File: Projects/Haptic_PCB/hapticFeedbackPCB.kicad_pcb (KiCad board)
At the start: 2 copper layers, 70.5 x 55 mm, 18 parts, among them J1 430450212, J2 430450212, M1 Motor_DC, M2 Motor_DC, M3 Motor_DC, Q1 NPN, Q2 NPN, Q3 NPN

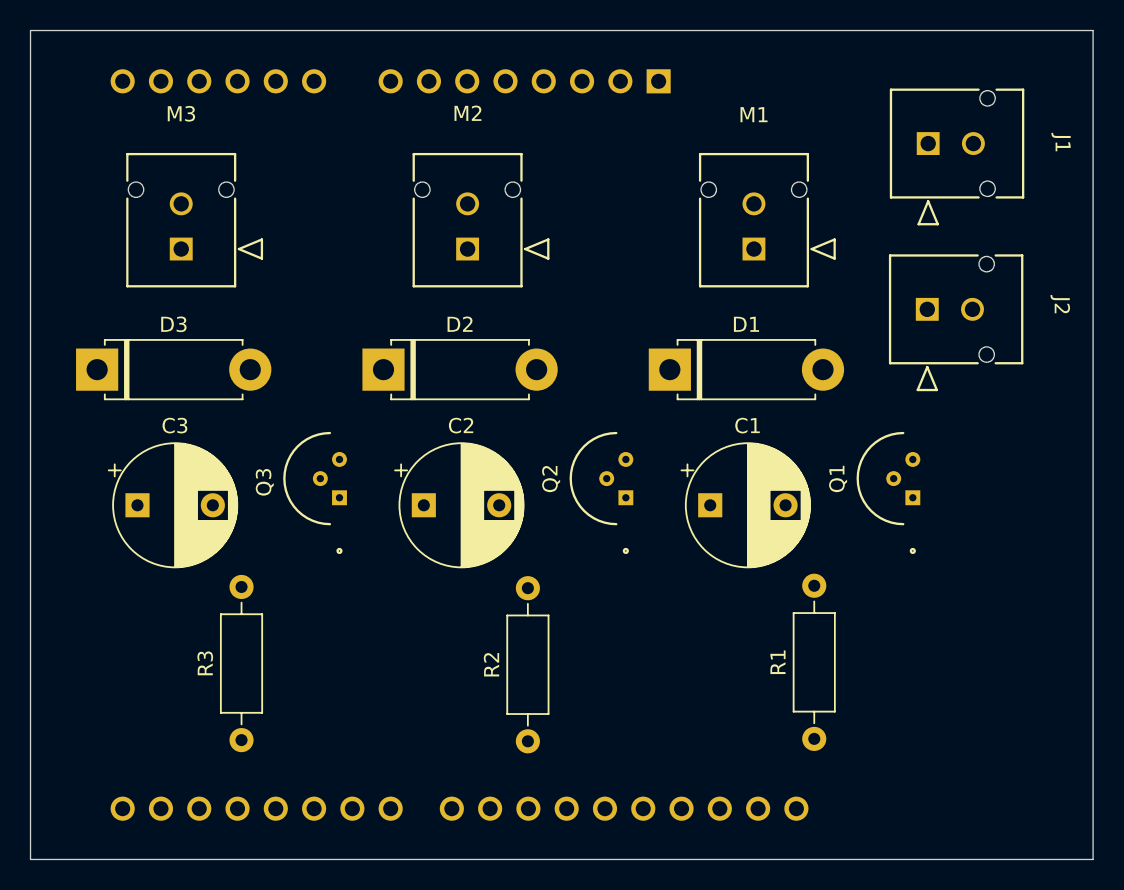
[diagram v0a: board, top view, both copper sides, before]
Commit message: Added PCB traces.
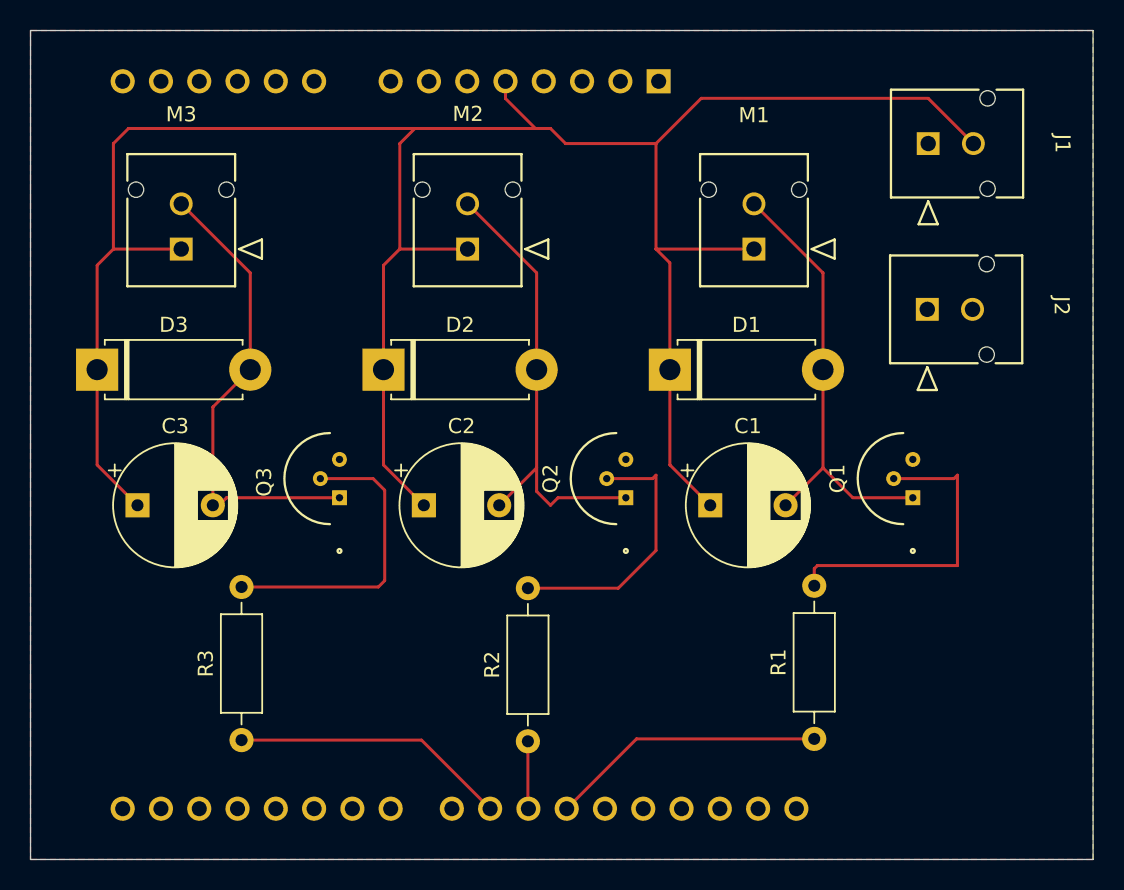
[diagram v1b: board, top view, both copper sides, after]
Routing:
- net +5V: track 0.00 -> 157.8 mm
- net Net-(D3-A): track 0.00 -> 31.5 mm
- net Net-(D2-A): track 0.00 -> 31.0 mm
- net Net-(D1-A): track 0.00 -> 30.2 mm
- net Net-(Q1-B): track 0.00 -> 21.0 mm
- net Net-(Q3-B): track 0.00 -> 20.3 mm
- net Net-(A1-D9): track 0.00 -> 18.4 mm
- net Net-(A1-D11): track 0.00 -> 18.3 mm
- net Net-(Q2-B): track 0.00 -> 17.9 mm
- net Net-(A1-D10): track 0.00 -> 4.48 mm
- added copper zone on F.Cu, net GND
